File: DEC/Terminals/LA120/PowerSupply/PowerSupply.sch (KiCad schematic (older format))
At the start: 61 parts, among them J1 Conn_01x12, J2 Conn_01x06, Q1 2N3791

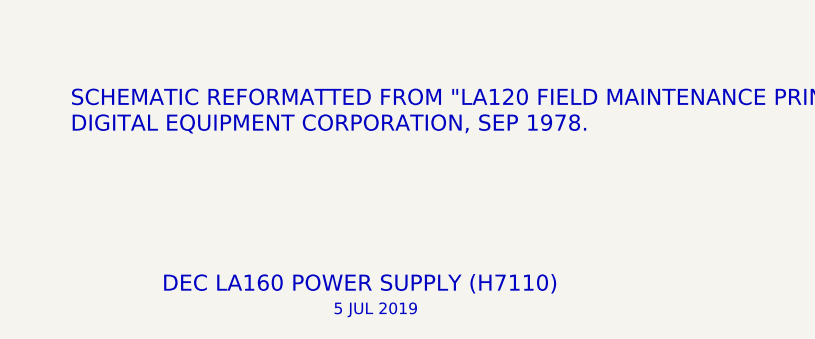
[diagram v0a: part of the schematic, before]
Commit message: Add readme, change name in schematic text block
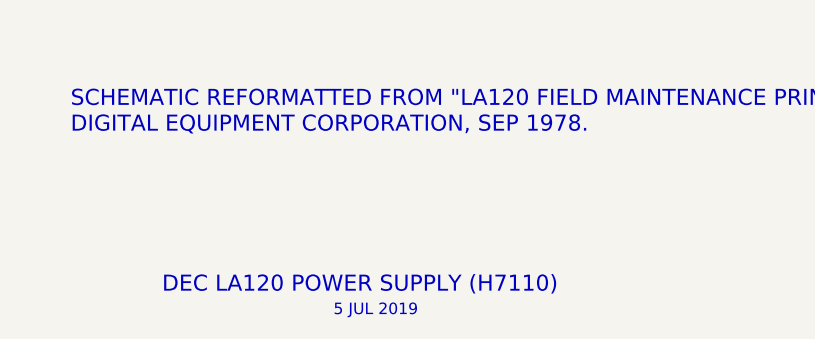
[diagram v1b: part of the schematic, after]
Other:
- note added: "DEC LA120 POWER SUPPLY (H7110)"
- note removed: "DEC LA160 POWER SUPPLY (H7110)"
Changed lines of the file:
@@
 EESchema Schematic File Version 4
+LIBS:PowerSupply-cache
 EELAYER 29 0
 EELAYER END
@@
 SCHEMATIC REFORMATTED FROM "LA120 FIELD MAINTENANCE PRINT SET",\nDIGITAL EQUIPMENT CORPORATION, SEP 1978.
 Text Notes 12250 10950 0    70   ~ 0
-DEC LA160 POWER SUPPLY (H7110)
+DEC LA120 POWER SUPPLY (H7110)
 Text Notes 13000 11050 0    50   ~ 0
 5 JUL 2019
